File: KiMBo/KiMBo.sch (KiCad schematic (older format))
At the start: 74 parts, among them CON1 μSD, P1 BED_THERM, P10 ENC, P11 Serial, P12 μUSB, P13 USB_Type_A, P14 Ethernet, P15 JTAG, P16 E_MOTOR, P17 H_MOTOR, P18 X0_MOTOR, P19 X1_MOTOR, P2 ADC, P20 Y0_MOTOR, P21 Y1_MOTOR, P22 Z0_MOTOR, P23 Z1_MOTOR, P24 Z2_MOTOR, P25 BED_HEAT, P26 E_HEAT, P27 H_HEAT, P28 DOCK0_HEAT, P29 DOCK1_HEAT, P3 TOOLHEAD0, P30 E_FAN, P31 H_FAN, P32 PWM, P33 CASE_FAN, P34 HS_FAN, P4 TOOLHEAD1, P5 DOCK0, P6 DOCK1, P7 X1, P8 Y2, P9 Z1, U1 MAX3370, X1 HDMI

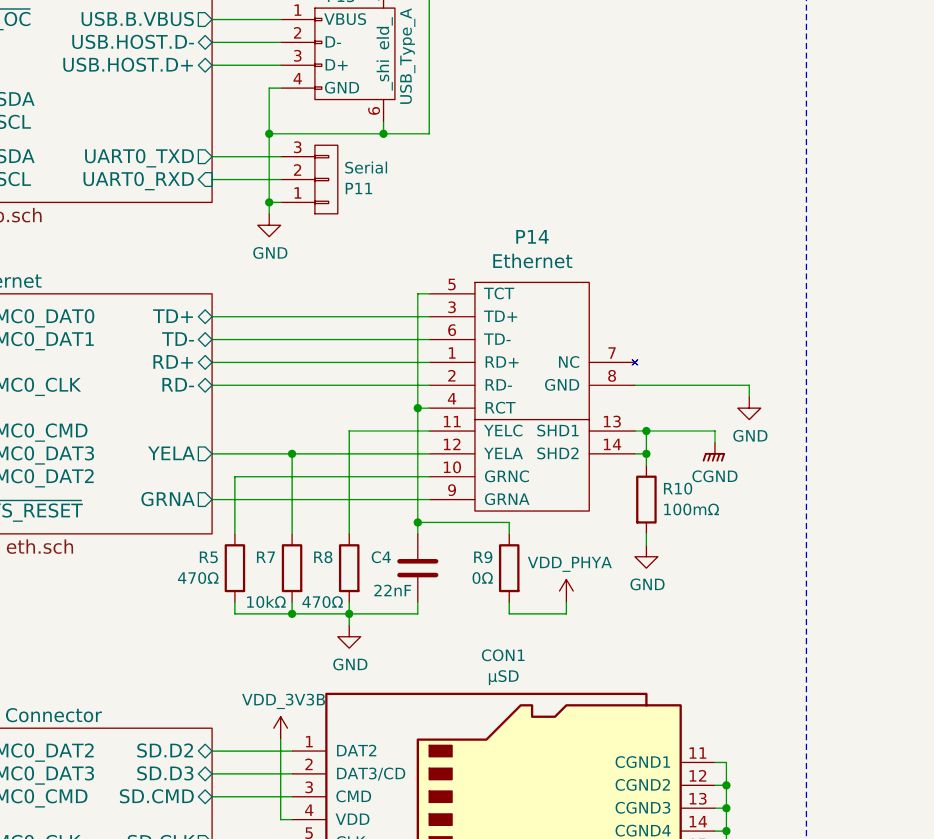
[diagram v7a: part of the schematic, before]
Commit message: Associate more footprints
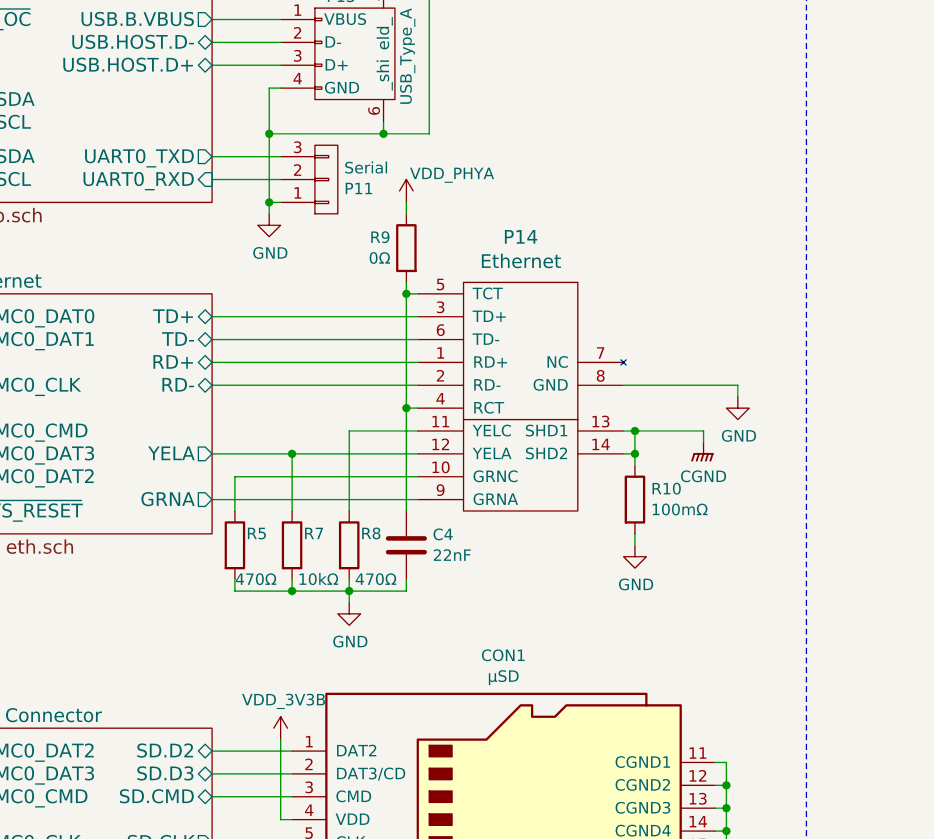
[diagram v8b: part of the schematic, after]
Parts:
- C1, C2: footprint Capacitors_SMD:C_0603 -> Capacitors_SMD:C_0402
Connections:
- net VDD_PHYA: now also R9.1; no longer R9.2
- net at C4.1, P14.4 (RCT), P14.5 (TCT): now also R9.2; no longer R9.1
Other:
- moved on the sheet: P14, R10, R5, R7, R8, R9
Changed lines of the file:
@@
 Sheet 1 26
 Title "KiMBo"
-Date "2017-03-07"
+Date "2017-03-17"
 Rev ""
 Comp "Aleph Objects Inc."
-Comment1 "CC-BY-SA 4.0, Copyright 2016"
+Comment1 "CC-BY-SA 4.0, Copyright 2016-2017"
 Comment2 ""
 Comment3 ""
@@
 L Ethernet_Connector P14
 U 1 1 58F00A29
-P 9600 3550
-F 0 "P14" H 9600 4247 60  0000 C CNN
-F 1 "Ethernet" H 9600 4141 60  0000 C CNN
-F 2 "" H 9600 4150 60  0001 C CNN
-F 3 "http://www.link-pp.com/?product/201411246424.html" H 9600 4150 60  0001 C CNN
-	1    9600 3550
+P 9550 3550
+F 0 "P14" H 9550 4247 60  0000 C CNN
+F 1 "Ethernet" H 9550 4141 60  0000 C CNN
+F 2 "" H 9550 4150 60  0001 C CNN
+F 3 "http://www.link-pp.com/?product/201411246424.html" H 9550 4150 60  0001 C CNN
+	1    9550 3550
 	1    0    0    -1
 $EndComp
@@
 L R R9
 U 1 1 58F00A30
-P 9500 4300
-F 0 "R9" H 9569 4346 50  0000 L CNN
-F 1 "0Ω" H 9569 4255 50  0000 L CNN
-F 2 "" V 9430 4300 50  0001 C CNN
-F 3 "" H 9500 4300 50  0000 C CNN
-	1    9500 4300
+P 9050 2900
+F 0 "R9" H 9119 2946 50  0000 L CNN
+F 1 "0Ω" H 9119 2855 50  0000 L CNN
+F 2 "" V 8980 2900 50  0001 C CNN
+F 3 "" H 9050 2900 50  0000 C CNN
+	1    9050 2900
 	-1   0    0    -1
 $EndComp
@@
 L CGND #PWR05
 U 1 1 58F00A37
-P 10400 3750
-F 0 "#PWR05" H 10400 3550 50  0001 C CNN
-F 1 "CGND" H 10400 3600 50  0000 C CNN
-F 2 "" H 10400 3700 50  0000 C CNN
-F 3 "" H 10400 3700 50  0000 C CNN
-	1    10400 3750
+P 10350 3750
+F 0 "#PWR05" H 10350 3550 50  0001 C CNN
+F 1 "CGND" H 10350 3600 50  0000 C CNN
+F 2 "" H 10350 3700 50  0000 C CNN
+F 3 "" H 10350 3700 50  0000 C CNN
+	1    10350 3750
 	1    0    0    -1
 $EndComp
@@
 L GND #PWR06
 U 1 1 58F00A3D
-P 10100 4200
-F 0 "#PWR06" H 10100 3950 50  0001 C CNN
-F 1 "GND" H 10105 4027 50  0000 C CNN
-F 2 "" H 10100 4200 50  0000 C CNN
-F 3 "" H 10100 4200 50  0000 C CNN
-	1    10100 4200
+P 10050 4200
+F 0 "#PWR06" H 10050 3950 50  0001 C CNN
+F 1 "GND" H 10055 4027 50  0000 C CNN
+F 2 "" H 10050 4200 50  0000 C CNN
+F 3 "" H 10050 4200 50  0000 C CNN
+	1    10050 4200
 	1    0    0    -1
 $EndComp
@@
 L R R10
 U 1 1 58F00A43
-P 10100 4000
-F 0 "R10" H 10170 4046 50  0000 L CNN
-F 1 "100mΩ" H 10170 3955 50  0000 L CNN
-F 2 "" V 10030 4000 50  0001 C CNN
-F 3 "" H 10100 4000 50  0000 C CNN
-	1    10100 4000
+P 10050 4000
+F 0 "R10" H 10120 4046 50  0000 L CNN
+F 1 "100mΩ" H 10120 3955 50  0000 L CNN
+F 2 "" V 9980 4000 50  0001 C CNN
+F 3 "" H 10050 4000 50  0000 C CNN
+	1    10050 4000
 	1    0    0    -1
 $EndComp
@@
 L GND #PWR07
 U 1 1 58F00A4A
-P 10550 3550
-F 0 "#PWR07" H 10550 3300 50  0001 C CNN
-F 1 "GND" H 10555 3377 50  0000 C CNN
-F 2 "" H 10550 3550 50  0000 C CNN
-F 3 "" H 10550 3550 50  0000 C CNN
-	1    10550 3550
+P 10500 3550
+F 0 "#PWR07" H 10500 3300 50  0001 C CNN
+F 1 "GND" H 10505 3377 50  0000 C CNN
+F 2 "" H 10500 3550 50  0000 C CNN
+F 3 "" H 10500 3550 50  0000 C CNN
+	1    10500 3550
 	1    0    0    -1
 $EndComp
@@
 L VDD_PHYA #PWR08
 U 1 1 58F00A50
-P 9750 4450
-F 0 "#PWR08" H 9750 4300 50  0001 C CNN
-F 1 "VDD_PHYA" H 9765 4623 50  0000 C CNN
-F 2 "" H 9750 4450 50  0000 C CNN
-F 3 "" H 9750 4450 50  0000 C CNN
-	1    9750 4450
+P 9050 2700
+F 0 "#PWR08" H 9050 2550 50  0001 C CNN
+F 1 "VDD_PHYA" H 9250 2825 50  0000 C CNN
+F 2 "" H 9050 2700 50  0000 C CNN
+F 3 "" H 9050 2700 50  0000 C CNN
+	1    9050 2700
 	1    0    0    -1
 $EndComp
@@
 $EndComp
 $Comp
-L C C4
-U 1 1 58FDAEA6
-P 9100 4300
-F 0 "C4" H 9214 4346 50  0000 L CNN
-F 1 "22nF" H 9125 4200 50  0000 L CNN
-F 2 "" H 9138 4150 50  0001 C CNN
-F 3 "" H 9100 4300 50  0000 C CNN
-	1    9100 4300
-	-1   0    0    -1
-$EndComp
-$Comp
 L GND #PWR010
 U 1 1 58FE07B8
-P 8800 4550
-F 0 "#PWR010" H 8800 4300 50  0001 C CNN
-F 1 "GND" H 8805 4377 50  0000 C CNN
-F 2 "" H 8800 4550 50  0000 C CNN
-F 3 "" H 8800 4550 50  0000 C CNN
-	1    8800 4550
+P 8800 4450
+F 0 "#PWR010" H 8800 4200 50  0001 C CNN
+F 1 "GND" H 8805 4277 50  0000 C CNN
+F 2 "" H 8800 4450 50  0000 C CNN
+F 3 "" H 8800 4450 50  0000 C CNN
+	1    8800 4450
 	1    0    0    -1
 $EndComp
@@
 L R R7
 U 1 1 592527AF
-P 8550 4300
-F 0 "R7" H 8619 4346 50  0000 L CNN
-F 1 "10kΩ" H 8575 4150 50  0000 L CNN
-F 2 "" V 8480 4300 50  0001 C CNN
-F 3 "" H 8550 4300 50  0000 C CNN
-	1    8550 4300
-	-1   0    0    -1
+P 8550 4200
+F 0 "R7" H 8600 4250 50  0000 L CNN
+F 1 "10kΩ" H 8575 4050 50  0000 L CNN
+F 2 "" V 8480 4200 50  0001 C CNN
+F 3 "" H 8550 4200 50  0000 C CNN
+	1    8550 4200
+	1    0    0    -1
 $EndComp
 $Comp
 L R R8
 U 1 1 59252A73
-P 8800 4300
-F 0 "R8" H 8869 4346 50  0000 L CNN
-F 1 "470Ω" H 8825 4150 50  0000 L CNN
-F 2 "" V 8730 4300 50  0001 C CNN
-F 3 "" H 8800 4300 50  0000 C CNN
-	1    8800 4300
-	-1   0    0    -1
+P 8800 4200
+F 0 "R8" H 8850 4250 50  0000 L CNN
+F 1 "470Ω" H 8825 4050 50  0000 L CNN
+F 2 "" V 8730 4200 50  0001 C CNN
+F 3 "" H 8800 4200 50  0000 C CNN
+	1    8800 4200
+	1    0    0    -1
 $EndComp
 $Comp
 L R R5
 U 1 1 59254D05
-P 8300 4300
-F 0 "R5" H 8369 4346 50  0000 L CNN
-F 1 "470Ω" H 8369 4255 50  0000 L CNN
-F 2 "" V 8230 4300 50  0001 C CNN
-F 3 "" H 8300 4300 50  0000 C CNN
-	1    8300 4300
-	-1   0    0    -1
+P 8300 4200
+F 0 "R5" H 8350 4250 50  0000 L CNN
+F 1 "470Ω" H 8300 4050 50  0000 L CNN
+F 2 "" V 8230 4200 50  0001 C CNN
+F 3 "" H 8300 4200 50  0000 C CNN
+	1    8300 4200
+	1    0    0    -1
 $EndComp
 Text Label 10500 10050 2    60   ~ 0
@@
 F 0 "C2" H 1614 6296 50  0000 L CNN
 F 1 "10nF" H 1614 6205 50  0000 L CNN
-F 2 "Capacitors_SMD:C_0603" H 1538 6100 50  0001 C CNN
+F 2 "Capacitors_SMD:C_0402" H 1538 6100 50  0001 C CNN
 F 3 "" H 1500 6250 50  0000 C CNN
 	1    1500 6250
@@
 F 0 "C1" H 1415 6296 50  0000 L CNN
 F 1 "100nF" H 1415 6205 50  0000 L CNN
-F 2 "Capacitors_SMD:C_0603" H 1338 6100 50  0001 C CNN
+F 2 "Capacitors_SMD:C_0402" H 1338 6100 50  0001 C CNN
 F 3 "" H 1300 6250 50  0000 C CNN
 	1    1300 6250
@@
 	10450 5150 10400 5150
 Wire Wire Line
-	9100 4100 9500 4100
-Wire Wire Line
-	9500 4100 9500 4150
-Wire Wire Line
-	10050 3700 10400 3700
-Wire Wire Line
-	10100 3700 10100 3850
-Wire Wire Line
-	10050 3800 10100 3800
-Connection ~ 10100 3800
-Wire Wire Line
-	10100 4200 10100 4150
-Wire Wire Line
-	10400 3700 10400 3750
-Connection ~ 10100 3700
-Wire Wire Line
-	10550 3550 10550 3500
-Wire Wire Line
-	10550 3500 10050 3500
-Wire Wire Line
-	9500 4450 9500 4500
-Wire Wire Line
-	9500 4500 9750 4500
-Wire Wire Line
-	9750 4500 9750 4450
+	10000 3700 10350 3700
+Wire Wire Line
+	10050 3700 10050 3850
+Wire Wire Line
+	10000 3800 10050 3800
+Connection ~ 10050 3800
+Wire Wire Line
+	10050 4200 10050 4150
+Wire Wire Line
+	10350 3700 10350 3750
+Connection ~ 10050 3700
+Wire Wire Line
+	10500 3550 10500 3500
+Wire Wire Line
+	10500 3500 10000 3500
 Wire Wire Line
 	8450 1700 8450 1600
@@
 	8500 5600 8550 5600
 Wire Wire Line
-	9150 3100 9100 3100
-Wire Wire Line
-	9100 3100 9100 4150
-Wire Wire Line
-	9100 3600 9150 3600
-Wire Wire Line
-	9100 4500 9100 4450
-Connection ~ 9100 3600
-Connection ~ 9100 4100
+	9100 3100 9050 3100
+Wire Wire Line
+	9050 3600 9100 3600
+Wire Wire Line
+	9050 4400 9050 4350
+Connection ~ 9050 3600
 Wire Wire Line
 	9450 9250 8200 9250
@@
 	8550 8100 8200 8100
 Wire Wire Line
-	9150 3200 8200 3200
-Wire Wire Line
-	9150 3300 8200 3300
-Wire Wire Line
-	9150 3400 8200 3400
-Wire Wire Line
-	9150 3500 8200 3500
-Wire Wire Line
-	8200 3800 9150 3800
-Wire Wire Line
-	9150 4000 8200 4000
+	9100 3200 8200 3200
+Wire Wire Line
+	9100 3300 8200 3300
+Wire Wire Line
+	9100 3400 8200 3400
+Wire Wire Line
+	9100 3500 8200 3500
+Wire Wire Line
+	8200 3800 9100 3800
+Wire Wire Line
+	9100 4000 8200 4000
 Wire Wire Line
 	2150 8650 2100 8650
@@
 	2250 10800 2100 10800
 Wire Wire Line
-	9150 3700 8800 3700
-Wire Wire Line
-	8800 3700 8800 4150
-Wire Wire Line
-	8550 3800 8550 4150
+	9100 3700 8800 3700
+Wire Wire Line
+	8800 3700 8800 4050
+Wire Wire Line
+	8550 3800 8550 4050
 Connection ~ 8550 3800
 Wire Wire Line
-	8300 3900 8300 4150
-Wire Wire Line
-	8300 4450 8300 4500
-Wire Wire Line
-	8300 4500 9100 4500
-Wire Wire Line
-	8800 4450 8800 4550
-Connection ~ 8800 4500
-Wire Wire Line
-	8550 4500 8550 4450
-Connection ~ 8550 4500
-Wire Wire Line
-	8300 3900 9150 3900
+	8300 3900 8300 4050
+Wire Wire Line
+	8300 4350 8300 4400
+Wire Wire Line
+	8300 4400 9050 4400
+Wire Wire Line
+	8800 4350 8800 4450
+Connection ~ 8800 4400
+Wire Wire Line
+	8550 4400 8550 4350
+Connection ~ 8550 4400
+Wire Wire Line
+	8300 3900 9100 3900
 Wire Wire Line
 	7100 3900 6550 3900
@@
 F 0 "C3" H 8415 10646 50  0000 L CNN
 F 1 "100nF" H 8415 10555 50  0000 L CNN
-F 2 "" H 8338 10450 50  0000 C CNN
+F 2 "" H 8338 10450 50  0001 C CNN
 F 3 "" H 8300 10600 50  0000 C CNN
 	1    8300 10600
@@
 F 0 "C5" H 9365 10646 50  0000 L CNN
 F 1 "100nF" H 9365 10555 50  0000 L CNN
-F 2 "" H 9288 10450 50  0000 C CNN
+F 2 "" H 9288 10450 50  0001 C CNN
 F 3 "" H 9250 10600 50  0000 C CNN
 	1    9250 10600
@@
 Text Notes 14800 1700 0    60   ~ 0
 EPM/Servo
+Connection ~ 9050 3100
+Wire Wire Line
+	9050 2750 9050 2700
+Wire Wire Line
+	9050 3050 9050 4050
+$Comp
+L C C4
+U 1 1 5910CA5D
+P 9050 4200
+F 0 "C4" H 9165 4246 50  0000 L CNN
+F 1 "22nF" H 9165 4155 50  0000 L CNN
+F 2 "" H 9088 4050 50  0001 C CNN
+F 3 "" H 9050 4200 50  0000 C CNN
+	1    9050 4200
+	1    0    0    -1
+$EndComp
 $EndSCHEMATC
